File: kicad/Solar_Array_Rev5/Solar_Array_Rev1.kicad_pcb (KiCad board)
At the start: 4 copper layers, 83 x 100 mm, 37 parts, among them IC1 TVS_4x4, IC2 SPV1040, IC4 TVS_4x4, P1 CONN_02X20, Q1 2N7002WT1GOSCT, Q2 NTR1P02T1GOSCT, Q3 MMBT3904, U1 LTC2990, U2 Solar_Panel

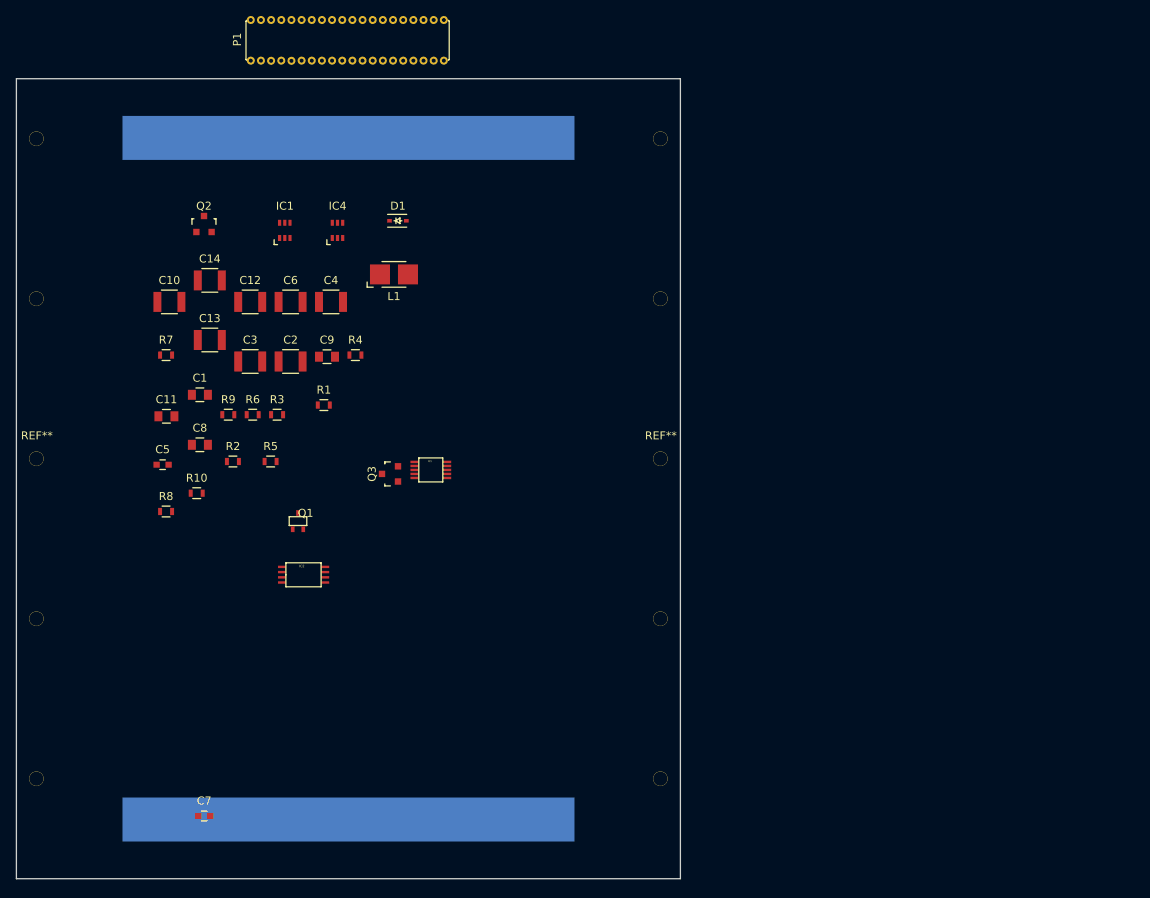
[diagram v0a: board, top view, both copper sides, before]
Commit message: Slight footprint adjustment.
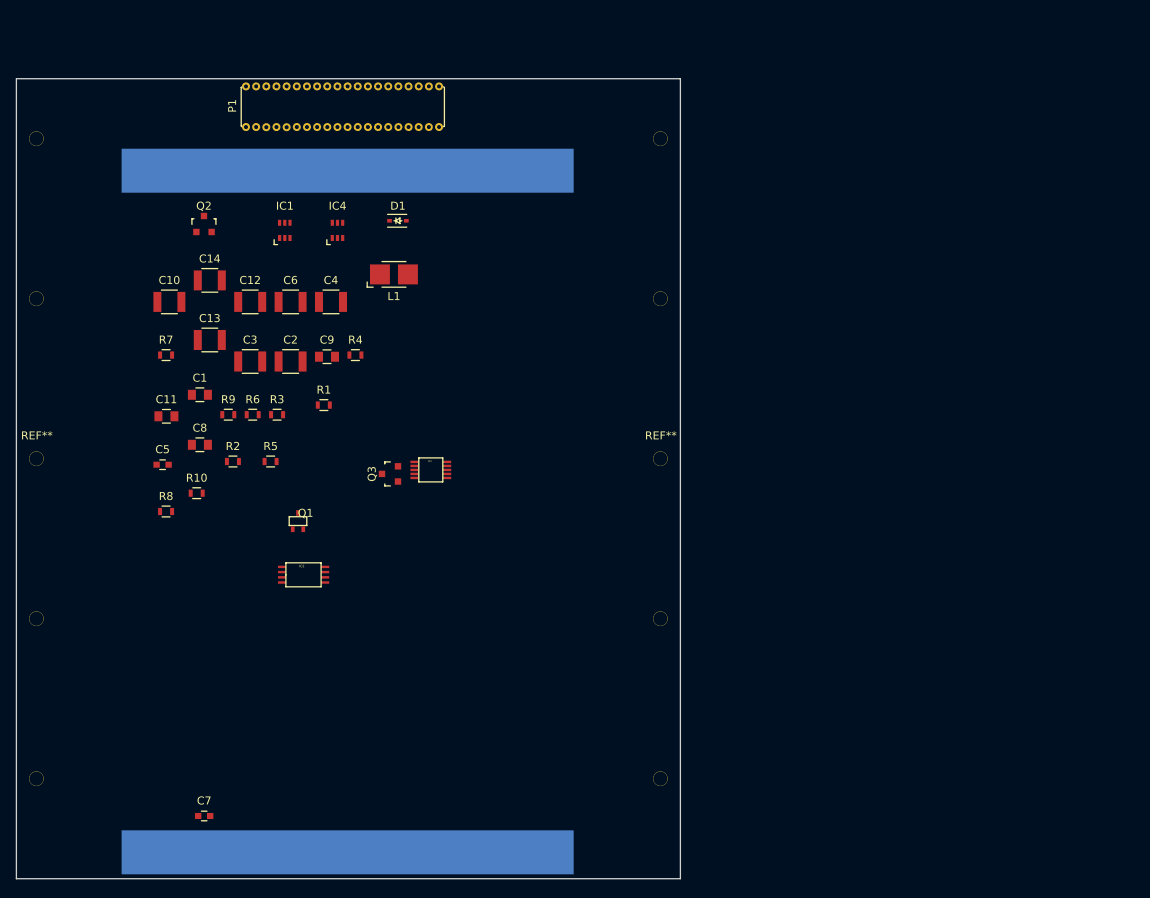
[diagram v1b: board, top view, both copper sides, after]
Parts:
- moved P1 8.32 mm to (151.4, 45.9)
- moved U2 4.10 mm to (151.4, 96.5)
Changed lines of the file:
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@@
     (links 84)
     (no_connects 84)
-    (area 109.949999 42.349999 193.050001 142.450001)
+    (area 106.070238 32.491666 197.429762 142.450001)
     (thickness 1.6)
     (drawings 4)
@@
   )
   (module Solar:ALTA_GA_CELL locked (layer B.Cu)
-    (at 151.5 92.4 180)
+    (at 151.4 96.5 180)
     (fp_text reference U2 (at 0 -0.5 180) (layer B.SilkS)
       (effects (font (size 1 1) (thickness 0.15)) (justify mirror))
@@
   )
   (module Solar:CS0_40PIN_HEADER (layer F.Cu)
-    (at 152 37.6 90)
+    (at 151.4 45.9 90)
     (fp_text reference P1 (at 0.1 -14.4 90) (layer F.SilkS)
       (effects (font (size 1 1) (thickness 0.15)))

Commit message: Routed PCB
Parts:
- L1: footprint Inductors:Inductor_1212 -> Solar:PNA4341.473NLT
- moved C7 44.2 mm to (154.2, 95.5), turned to 270 degrees
- moved D1 36.4 mm to (150.2, 95.8), turned to 90 degrees
- moved R7 33.0 mm to (156.1, 95.4), turned to 90 degrees
- moved R10 32.3 mm to (162.9, 83.1), turned to 270 degrees
- moved L1 31.5 mm to (143.7, 95.3)
- moved R8 29.4 mm to (158.1, 95.4), turned to 90 degrees
- moved C6 28.6 mm to (132.2, 96.2), turned to 180 degrees
- moved C4 28.1 mm to (132.2, 92.6), turned to 180 degrees
- moved C8 27.5 mm to (160.2, 92.0), turned to 270 degrees
- moved Q2 26.7 mm to (141.7, 85.9), turned to 180 degrees
- moved C11 23.6 mm to (152.0, 80.3)
- moved C5 20.6 mm to (148.8, 88.9), turned to 90 degrees
- moved R6 20.3 mm to (158.1, 92.5), turned to 90 degrees
- moved C2 19.8 mm to (137.2, 96.2), turned to 180 degrees
- moved C9 19.2 mm to (140.9, 59.7), turned to 180 degrees
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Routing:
- net Net-(IC1-Pad3): track 0.00 -> 421.0 mm, vias 0 -> 19
- net Net-(IC1-Pad4): track 0.00 -> 59.9 mm, vias 0 -> 3
- net Net-(IC4-Pad1): track 0.00 -> 59.2 mm, vias 0 -> 3
- net Net-(C10-Pad1): track 0.00 -> 59.2 mm, vias 0 -> 4
- net Net-(IC4-Pad3): track 0.00 -> 56.3 mm, vias 0 -> 2
- net Net-(IC4-Pad4): track 0.00 -> 54.3 mm, vias 0 -> 2
- net Net-(IC4-Pad6): track 0.00 -> 53.6 mm, vias 0 -> 2
- net Net-(IC1-Pad1): track 0.00 -> 47.4 mm, vias 0 -> 2
- net Net-(C1-Pad1): track 0.00 -> 28.6 mm
- net (no net): track 0.00 -> 19.6 mm
- net Net-(D1-Pad1): track 0.00 -> 15.1 mm
- net Net-(C11-Pad1): track 0.00 -> 11.3 mm
- net GND: track 0.00 -> 10.4 mm, vias 0 -> 19
- net Net-(C8-Pad2): track 0.00 -> 9.81 mm, vias 0 -> 2
- net Net-(Q1-Pad1): track 0.00 -> 8.82 mm
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- added copper zone on In1.Cu, net GND
- added copper zone on In2.Cu, net Net-(IC1-Pad3)
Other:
- net class MID POWER BUS added: clearance 0.2, trace_width 2, via_dia 1, via_drill 0.8
- net class TOPThick added: clearance 0.2, trace_width 0.3, via_dia 0.6, via_drill 0.4
- net class Top added: clearance 0.1, trace_width 0.27, via_dia 0.6, via_drill 0.4

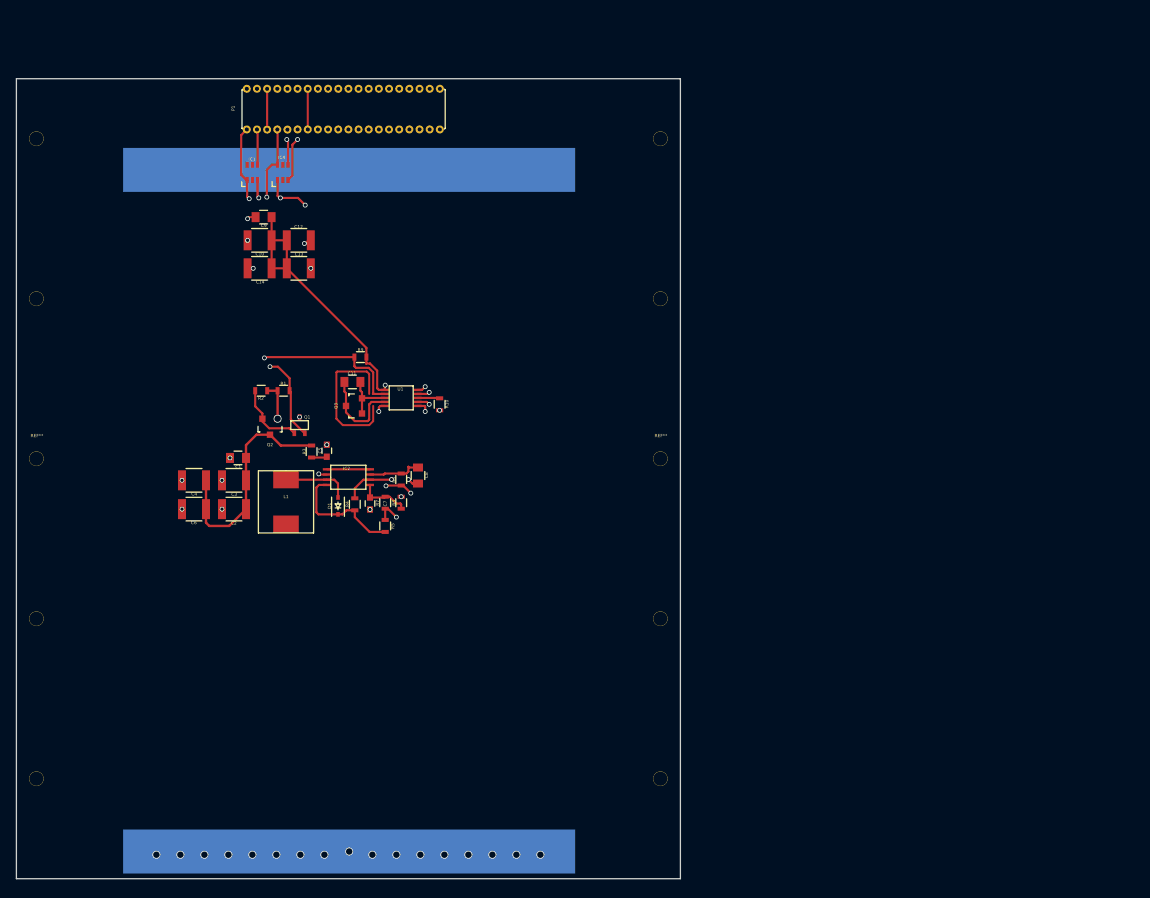
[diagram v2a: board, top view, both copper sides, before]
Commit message: Added Mechanical drawings/folder. Finished layout. -Added /mechanical to /solar -Added solar stl -Finished layout
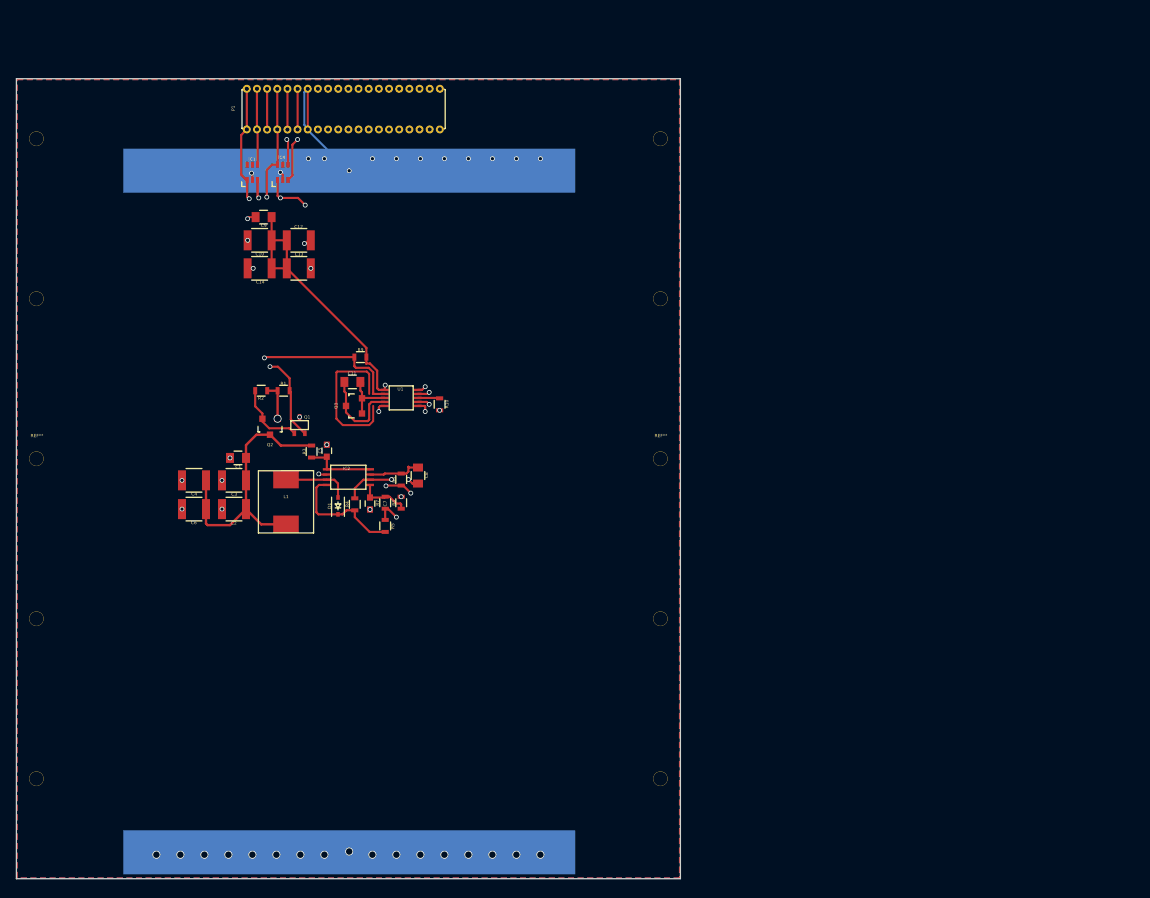
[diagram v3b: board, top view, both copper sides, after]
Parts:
- moved U2 0.10 mm to (151.6, 96.5)
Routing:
- net GND: track 10.4 -> 241.4 mm, vias 19 -> 32
- net Net-(C1-Pad1): track 28.6 -> 34.4 mm
- net Net-(IC4-Pad6): track 53.6 -> 59.1 mm, vias 2 -> 4
- net Net-(IC4-Pad1): track 59.2 -> 64.6 mm, vias 3 -> 5
- net Net-(IC4-Pad4): track 54.3 -> 59.8 mm, vias 2 -> 4
- net Net-(IC1-Pad4): track 59.9 -> 65.3 mm
- net Net-(IC1-Pad1): track 47.4 -> 52.8 mm, vias 2 -> 4
- net Net-(IC4-Pad3): track 56.3 -> 61.7 mm, vias 2 -> 4
- net Net-(C5-Pad1): track 7.34 -> 8.92 mm
- added copper zone on B.Cu, net GND
- added copper zone on F.Cu, net GND
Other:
- net class BOTGND added: clearance 0.2, trace_width 2, via_dia 1, via_drill 0.4

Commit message: Started transcription from kicad to Eagle  -Added RCL to board  -Added stand-in parts for p/n fets  -Started nets.
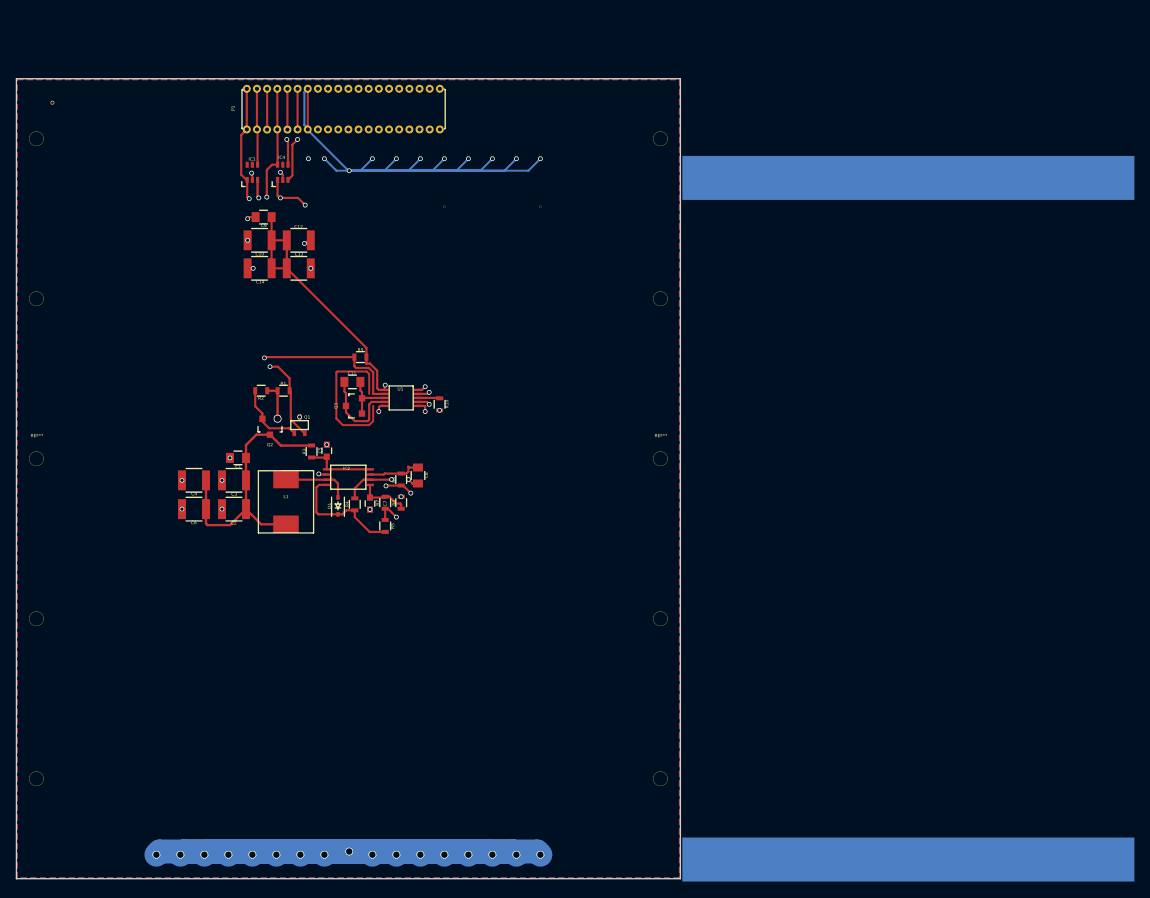
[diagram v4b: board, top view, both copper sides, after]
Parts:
- added REF**: GND_VIA, Solar:GND_VIA, F.Cu at (114.5, 45.4)
- added REF**: GND_VIA, Solar:GND_VIA, F.Cu at (175.5, 58.4)
- added REF**: GND_VIA, Solar:GND_VIA, F.Cu at (163.5, 58.4)
- moved U2 69.9 mm to (221.5, 97.4)
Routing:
- net Net-(IC1-Pad3): track 421.0 -> 35.7 mm, vias 19 -> 2
- net (no net): track 19.6 -> 404.9 mm, vias 0 -> 17
